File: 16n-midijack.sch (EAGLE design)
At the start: 21 parts

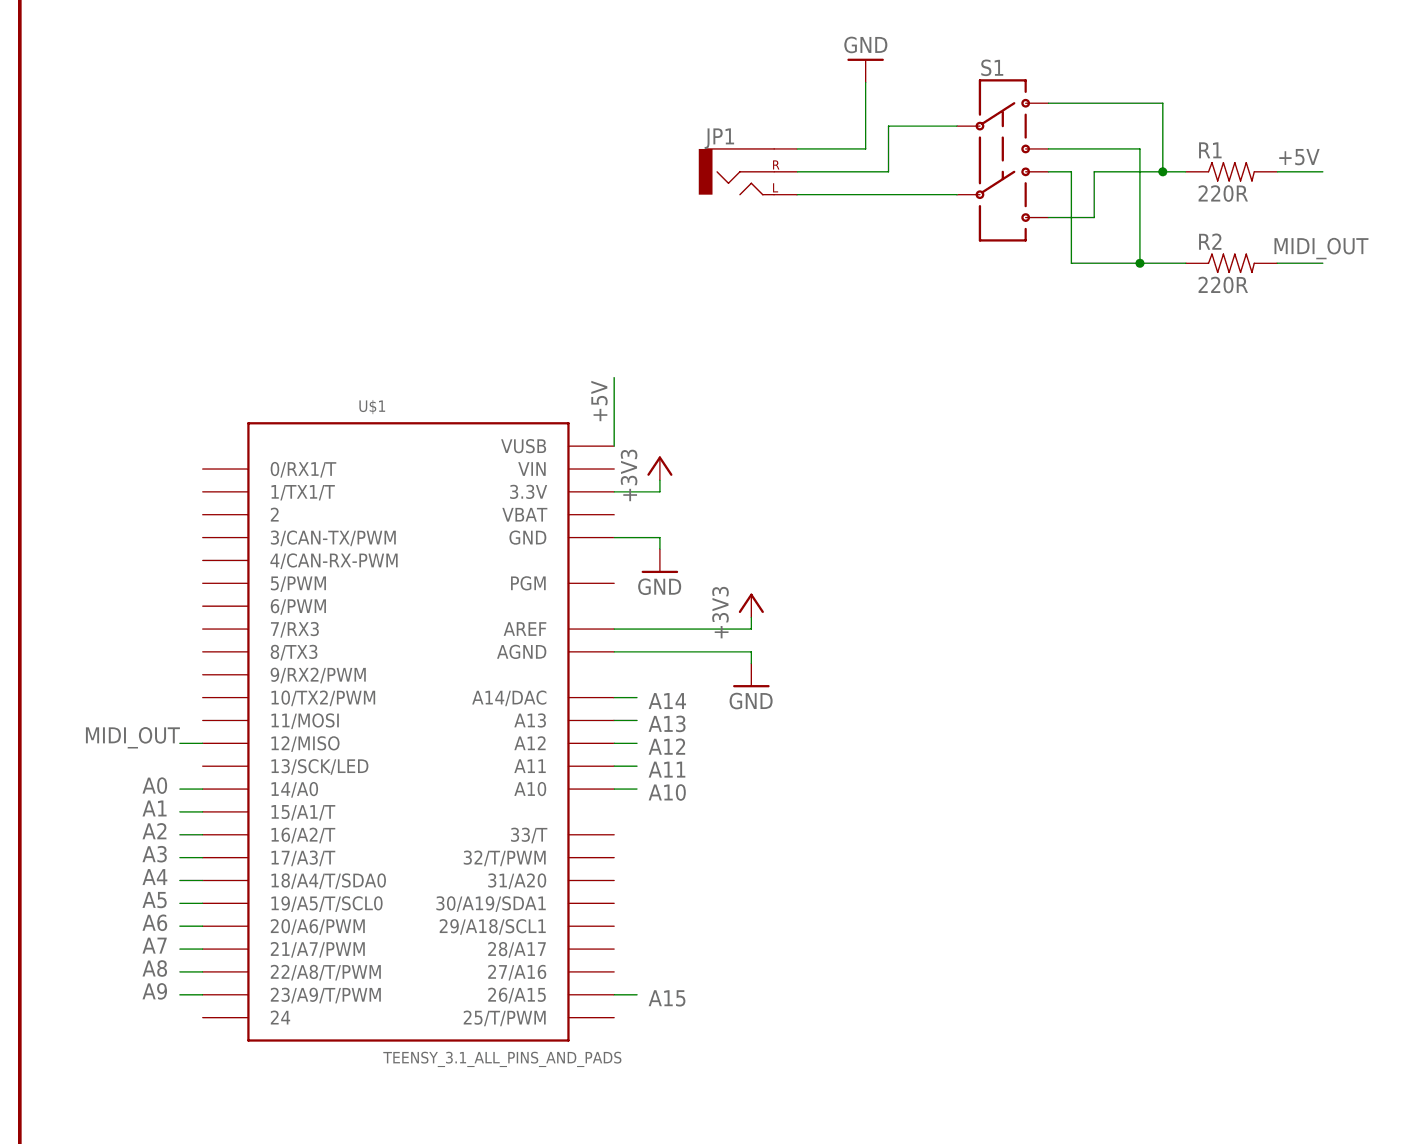
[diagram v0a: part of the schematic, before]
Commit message: SPI and MIDI breakouts.
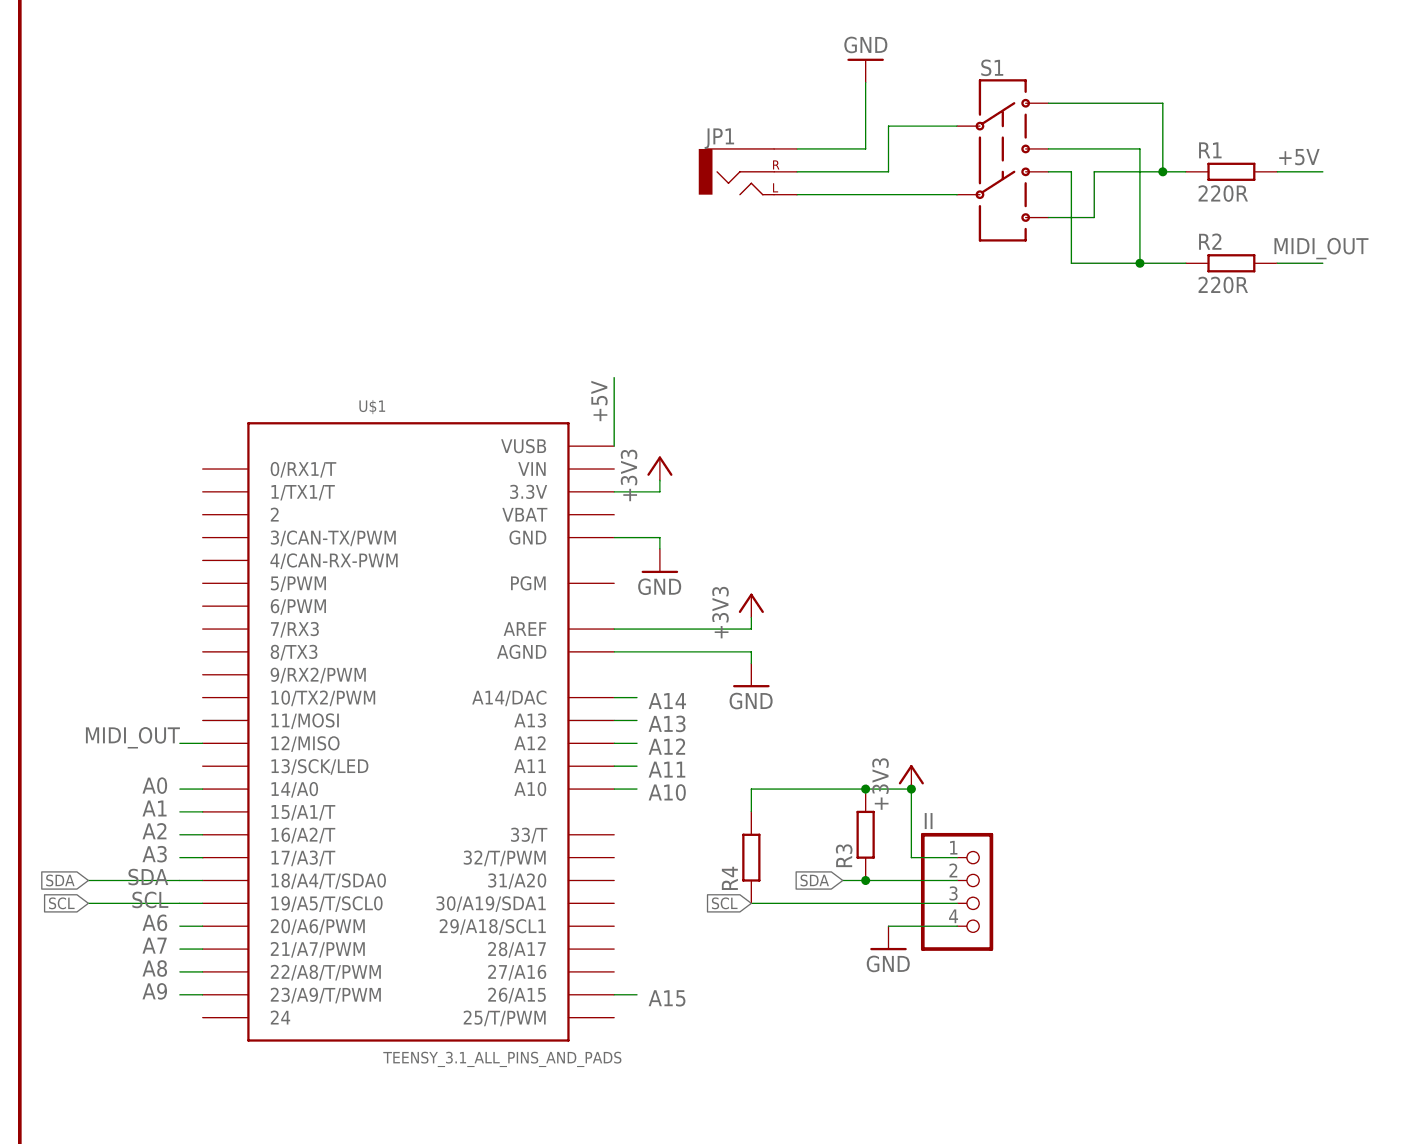
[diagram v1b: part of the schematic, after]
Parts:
- added II: (no value), pinhead:PINHD-1X4/90
- added R3, R4: (no value), rcl:R-EU_R0805
- R1, R2: device SparkFun-Resistors:RESISTOR1206 -> rcl:R-EU_R0805
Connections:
- new net SCL: II.3, R4.1, U$1.19/A5/T/SCL0
- new net SDA: II.2, R3.1, U$1.18/A4/T/SDA0
- net +3V3: now also II.1, R3.2, R4.2
- net A4: no longer U$1.18/A4/T/SDA0
- net A5: no longer U$1.19/A5/T/SCL0
- net GND: now also II.4
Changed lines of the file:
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@@
 <?xml version="1.0" encoding="utf-8"?>
 <!DOCTYPE eagle SYSTEM "eagle.dtd">
-<eagle version="8.3.1">
+<eagle version="8.4.1">
 <drawing>
 <settings>
@@
 <part name="+3V16" library="supply1" deviceset="+3V3" device=""/>
 <part name="U$17" library="monome" deviceset="SLIDEPOT-ALPS-60MM" device=""/>
-<part name="R1" library="SparkFun-Resistors" deviceset="RESISTOR" device="1206" value="220R"/>
-<part name="R2" library="SparkFun-Resistors" deviceset="RESISTOR" device="1206" value="220R"/>
+<part name="R1" library="rcl" library_urn="urn:adsk.eagle:library:334" deviceset="R-EU_" device="R0805" package3d_urn="urn:adsk.eagle:package:23553/2" value="220R"/>
+<part name="R2" library="rcl" library_urn="urn:adsk.eagle:library:334" deviceset="R-EU_" device="R0805" package3d_urn="urn:adsk.eagle:package:23553/2" value="220R"/>
 <part name="JP1" library="SparkFun-Connectors" deviceset="AUDIO-JACK" device="PTH"/>
 <part name="GND17" library="supply1" deviceset="GND" device=""/>
 <part name="S1" library="SparkFun-Electromechanical" deviceset="SWITCH-DPDT" device="EG2211"/>
+<part name="II" library="pinhead" library_urn="urn:adsk.eagle:library:325" deviceset="PINHD-1X4" device="/90" package3d_urn="urn:adsk.eagle:package:22404/1"/>
+<part name="GND19" library="supply1" deviceset="GND" device=""/>
+<part name="+3V18" library="supply1" deviceset="+3V3" device=""/>
+<part name="R3" library="rcl" library_urn="urn:adsk.eagle:library:334" deviceset="R-EU_" device="R0805" package3d_urn="urn:adsk.eagle:package:23553/2"/>
+<part name="R4" library="rcl" library_urn="urn:adsk.eagle:library:334" deviceset="R-EU_" device="R0805" package3d_urn="urn:adsk.eagle:package:23553/2"/>
 </parts>
 <sheets>
@@
 <instance part="GND17" gate="1" x="93.98" y="124.206" rot="R180"/>
 <instance part="S1" gate="G$1" x="109.22" y="114.3"/>
+<instance part="II" gate="A" x="106.68" y="30.48"/>
+<instance part="GND19" gate="1" x="96.52" y="25.4"/>
+<instance part="+3V18" gate="G$1" x="99.06" y="45.72"/>
+<instance part="R3" gate="G$1" x="93.98" y="38.1" rot="R90"/>
+<instance part="R4" gate="G$1" x="81.28" y="35.56" rot="R90"/>
 </instances>
 <busses>
@@
 <wire x1="93.98" y1="114.3" x2="93.98" y2="121.666" width="0.1524" layer="91"/>
 </segment>
+<segment>
+<pinref part="II" gate="A" pin="4"/>
+<wire x1="104.14" y1="27.94" x2="96.52" y2="27.94" width="0.1524" layer="91"/>
+<pinref part="GND19" gate="1" pin="GND"/>
+</segment>
 </net>
 <net name="+3V3" class="0">
@@
 <pinref part="+3V16" gate="G$1" pin="+3V3"/>
 </segment>
+<segment>
+<pinref part="R4" gate="G$1" pin="2"/>
+<wire x1="81.28" y1="40.64" x2="81.28" y2="43.18" width="0.1524" layer="91"/>
+<pinref part="R3" gate="G$1" pin="2"/>
+<wire x1="81.28" y1="43.18" x2="93.98" y2="43.18" width="0.1524" layer="91"/>
+<pinref part="+3V18" gate="G$1" pin="+3V3"/>
+<wire x1="93.98" y1="43.18" x2="99.06" y2="43.18" width="0.1524" layer="91"/>
+<junction x="93.98" y="43.18"/>
+<pinref part="II" gate="A" pin="1"/>
+<wire x1="104.14" y1="35.56" x2="99.06" y2="35.56" width="0.1524" layer="91"/>
+<wire x1="99.06" y1="35.56" x2="99.06" y2="43.18" width="0.1524" layer="91"/>
+<junction x="99.06" y="43.18"/>
+</segment>
 </net>
 <net name="A0" class="0">
@@
 <net name="A4" class="0">
 <segment>
-<pinref part="U$1" gate="G$1" pin="18/A4/T/SDA0"/>
-<wire x1="17.78" y1="33.02" x2="20.32" y2="33.02" width="0.1524" layer="91"/>
-<label x="16.51" y="34.29" size="1.778" layer="95" rot="R180"/>
-</segment>
-<segment>
 <pinref part="U$6" gate="G$1" pin="2"/>
 <wire x1="91.44" y1="160.02" x2="93.98" y2="160.02" width="0.1524" layer="91"/>
@@
 </net>
 <net name="A5" class="0">
-<segment>
-<pinref part="U$1" gate="G$1" pin="19/A5/T/SCL0"/>
-<wire x1="17.78" y1="30.48" x2="20.32" y2="30.48" width="0.1524" layer="91"/>
-<label x="16.51" y="31.75" size="1.778" layer="95" rot="R180"/>
-</segment>
 <segment>
 <pinref part="U$7" gate="G$1" pin="2"/>
@@
 </segment>
 </net>
+<net name="SDA" class="0">
+<segment>
+<pinref part="U$1" gate="G$1" pin="18/A4/T/SDA0"/>
+<wire x1="17.78" y1="33.02" x2="20.32" y2="33.02" width="0.1524" layer="91"/>
+<label x="16.51" y="34.29" size="1.778" layer="95" rot="R180"/>
+<wire x1="17.78" y1="33.02" x2="7.62" y2="33.02" width="0.1524" layer="91"/>
+<label x="7.62" y="33.02" size="1.27" layer="95" rot="R180" xref="yes"/>
+</segment>
+<segment>
+<pinref part="II" gate="A" pin="2"/>
+<wire x1="104.14" y1="33.02" x2="93.98" y2="33.02" width="0.1524" layer="91"/>
+<label x="91.44" y="33.02" size="1.27" layer="95" rot="R180" xref="yes"/>
+<pinref part="R3" gate="G$1" pin="1"/>
+<wire x1="93.98" y1="33.02" x2="91.44" y2="33.02" width="0.1524" layer="91"/>
+<junction x="93.98" y="33.02"/>
+</segment>
+</net>
+<net name="SCL" class="0">
+<segment>
+<pinref part="U$1" gate="G$1" pin="19/A5/T/SCL0"/>
+<wire x1="17.78" y1="30.48" x2="20.32" y2="30.48" width="0.1524" layer="91"/>
+<label x="16.51" y="31.75" size="1.778" layer="95" rot="R180"/>
+<wire x1="17.78" y1="30.48" x2="7.62" y2="30.48" width="0.1524" layer="91"/>
+<label x="7.62" y="30.48" size="1.27" layer="95" rot="R180" xref="yes"/>
+</segment>
+<segment>
+<pinref part="II" gate="A" pin="3"/>
+<wire x1="104.14" y1="30.48" x2="81.28" y2="30.48" width="0.1524" layer="91"/>
+<label x="81.28" y="30.48" size="1.27" layer="95" rot="R180" xref="yes"/>
+<pinref part="R4" gate="G$1" pin="1"/>
+</segment>
+</net>
 </nets>
 </sheet>
@@
 </schematic>
 </drawing>
+<compatibility>
+<note version="8.2" severity="warning">
+Since Version 8.2, EAGLE supports online libraries. The ids
+of those online libraries will not be understood (or retained)
+with this version.
+</note>
+<note version="8.3" severity="warning">
+Since Version 8.3, EAGLE supports URNs for individual library
+assets (packages, symbols, and devices). The URNs of those assets
+will not be understood (or retained) with this version.
+</note>
+<note version="8.3" severity="warning">
+Since Version 8.3, EAGLE supports the association of 3D packages
+with devices in libraries, schematics, and board files. Those 3D
+packages will not be understood (or retained) with this version.
+</note>
+</compatibility>
 </eagle>

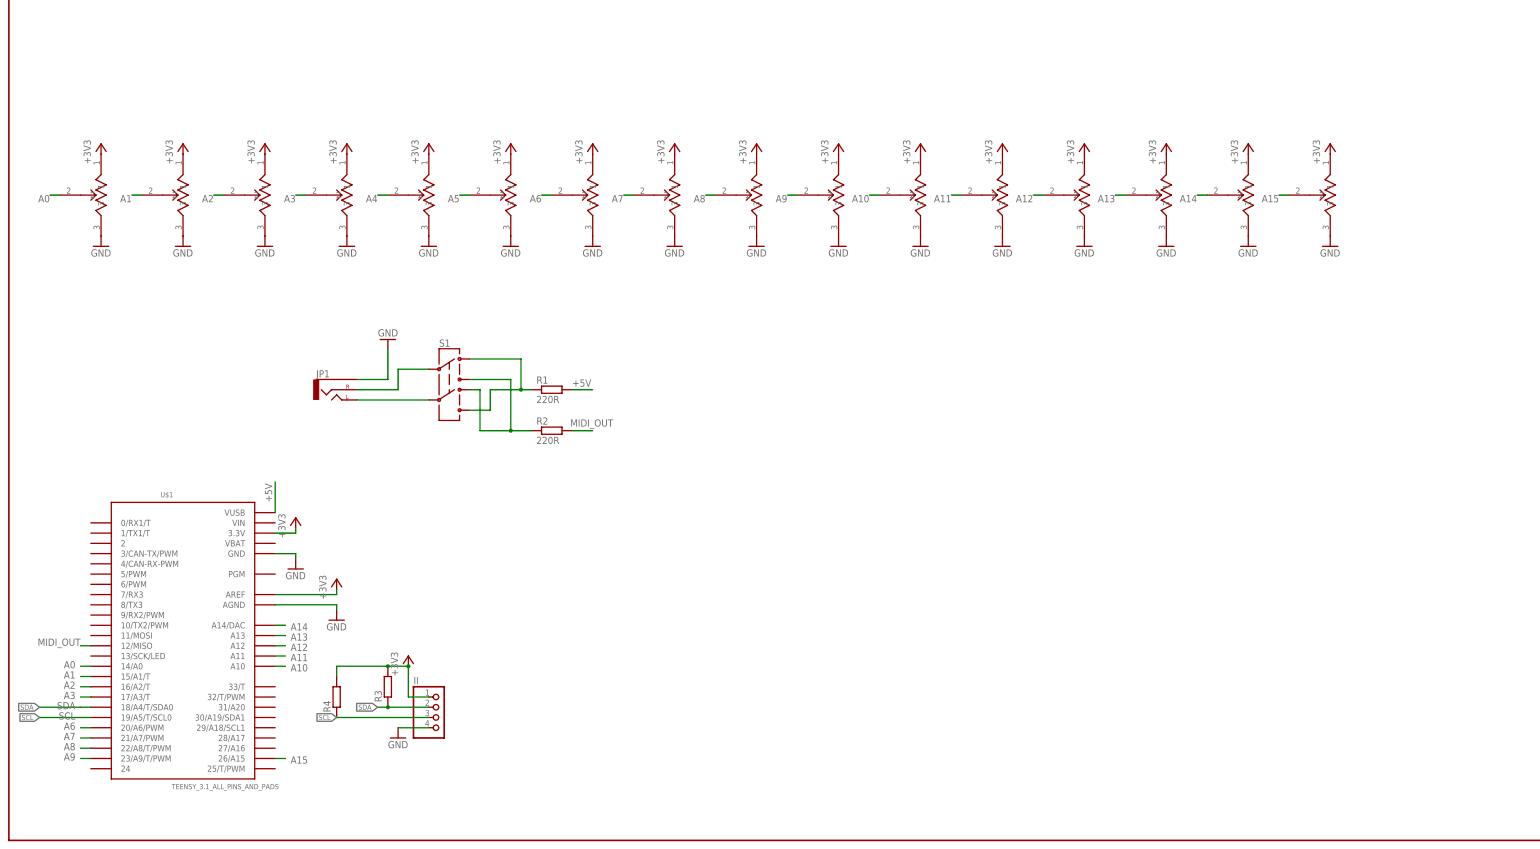
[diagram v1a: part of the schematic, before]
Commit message: Various changes:
- through hole componentry
- up-to-date silking
- protection diodes on II lines
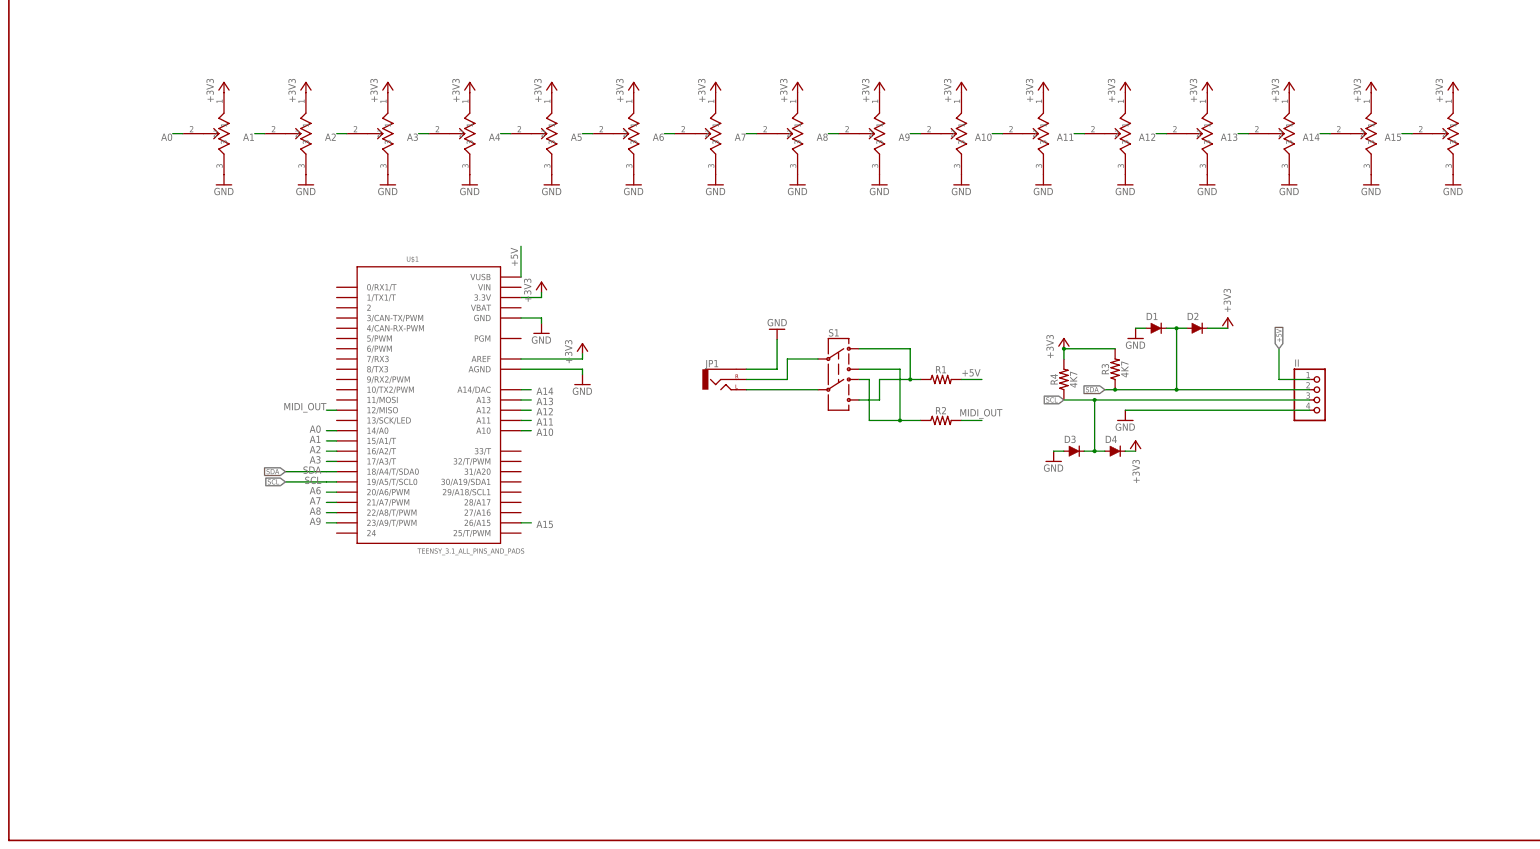
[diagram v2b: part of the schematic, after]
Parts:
- added D1, D2, D3, D4: DIODE-1N4148, SparkFun-DiscreteSemi:DIODE-1N4148
- R1, R2: value 220R -> (none); device rcl:R-EU_R0805 -> SparkFun-Resistors:RESISTORAXIAL-0.3-KIT
- R3, R4: value (none) -> 4K7; device rcl:R-EU_R0805 -> SparkFun-Resistors:RESISTORAXIAL-0.3-KIT
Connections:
- net +3V3: now also D2.C, D4.C; no longer II.1
- net +5V: now also II.1
- net GND: now also D1.A, D3.A
- net SCL: now also D3.C, D4.A
- net SDA: now also D1.C, D2.A
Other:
- moved on the sheet: II, JP1, S1, U$1

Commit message: What I sent to Sean.
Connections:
- net MIDI_OUT: now also U$1.10/TX2/PWM; no longer U$1.12/MISO
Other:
- note added: "I2C Breakout"
- note added: "Minijack-MIDI and Protocol Switching"
- note added: "Teensy"
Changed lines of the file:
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@@
 <layer number="230" name="230bmp" color="7" fill="1" visible="yes" active="yes"/>
 <layer number="231" name="231bmp" color="7" fill="1" visible="yes" active="yes"/>
+<layer number="232" name="Eagle3D_PG2" color="7" fill="1" visible="no" active="no"/>
+<layer number="233" name="Eagle3D_PG3" color="7" fill="1" visible="no" active="no"/>
 <layer number="248" name="Housing" color="7" fill="1" visible="yes" active="yes"/>
 <layer number="249" name="Edge" color="7" fill="1" visible="yes" active="yes"/>
@@
 <part name="+3V20" library="supply1" deviceset="+3V3" device=""/>
 <part name="+3V21" library="supply1" deviceset="+3V3" device=""/>
+<part name="SUPPLY1" library="supply2" library_urn="urn:adsk.eagle:library:372" deviceset="+5V" device=""/>
 </parts>
 <sheets>
 <sheet>
 <plain>
+<text x="96.52" y="63.5" size="2.54" layer="91">Teensy</text>
+<text x="195.58" y="63.5" size="2.54" layer="91">Minijack-MIDI and
+Protocol Switching</text>
+<text x="284.48" y="63.5" size="2.54" layer="91">I2C Breakout</text>
 </plain>
 <instances>
@@
 <attribute name="VALUE" x="280.416" y="88.392" size="1.778" layer="96" rot="R90"/>
 </instance>
+<instance part="SUPPLY1" gate="+5V" x="314.96" y="119.38"/>
 </instances>
 <busses>
@@
 <pinref part="II" gate="A" pin="1"/>
 <wire x1="322.58" y1="114.3" x2="314.96" y2="114.3" width="0.1524" layer="91"/>
-<wire x1="314.96" y1="114.3" x2="314.96" y2="121.92" width="0.1524" layer="91"/>
-<label x="314.96" y="121.92" size="1.27" layer="95" rot="R90" xref="yes"/>
+<pinref part="SUPPLY1" gate="+5V" pin="+5V"/>
+<wire x1="314.96" y1="116.84" x2="314.96" y2="114.3" width="0.1524" layer="91"/>
 </segment>
 </net>
@@
 <net name="MIDI_OUT" class="0">
 <segment>
-<pinref part="U$1" gate="G$1" pin="12/MISO"/>
-<wire x1="81.28" y1="106.68" x2="78.74" y2="106.68" width="0.1524" layer="91"/>
-<label x="78.74" y="108.458" size="1.778" layer="95" rot="R180"/>
-</segment>
-<segment>
 <pinref part="R2" gate="G$1" pin="2"/>
 <wire x1="236.22" y1="104.14" x2="241.3" y2="104.14" width="0.1524" layer="91"/>
 <label x="235.712" y="105.156" size="1.778" layer="95"/>
+</segment>
+<segment>
+<pinref part="U$1" gate="G$1" pin="10/TX2/PWM"/>
+<wire x1="81.28" y1="111.76" x2="73.66" y2="111.76" width="0.1524" layer="91"/>
+<label x="73.66" y="111.76" size="1.27" layer="95" rot="R180" xref="yes"/>
 </segment>
 </net>
@@
 </drawing>
 <compatibility>
+<note version="6.3" minversion="6.2.2" severity="warning">
+Since Version 6.2.2 text objects can contain more than one line,
+which will not be processed correctly with this version.
+</note>
 <note version="8.2" severity="warning">
 Since Version 8.2, EAGLE supports online libraries. The ids
